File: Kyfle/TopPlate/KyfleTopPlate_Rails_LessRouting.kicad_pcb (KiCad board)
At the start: 2 copper layers, 164 x 146.3 mm, 66 parts, among them SW2 KEY_SWITCH, SW2 PRO MICRO

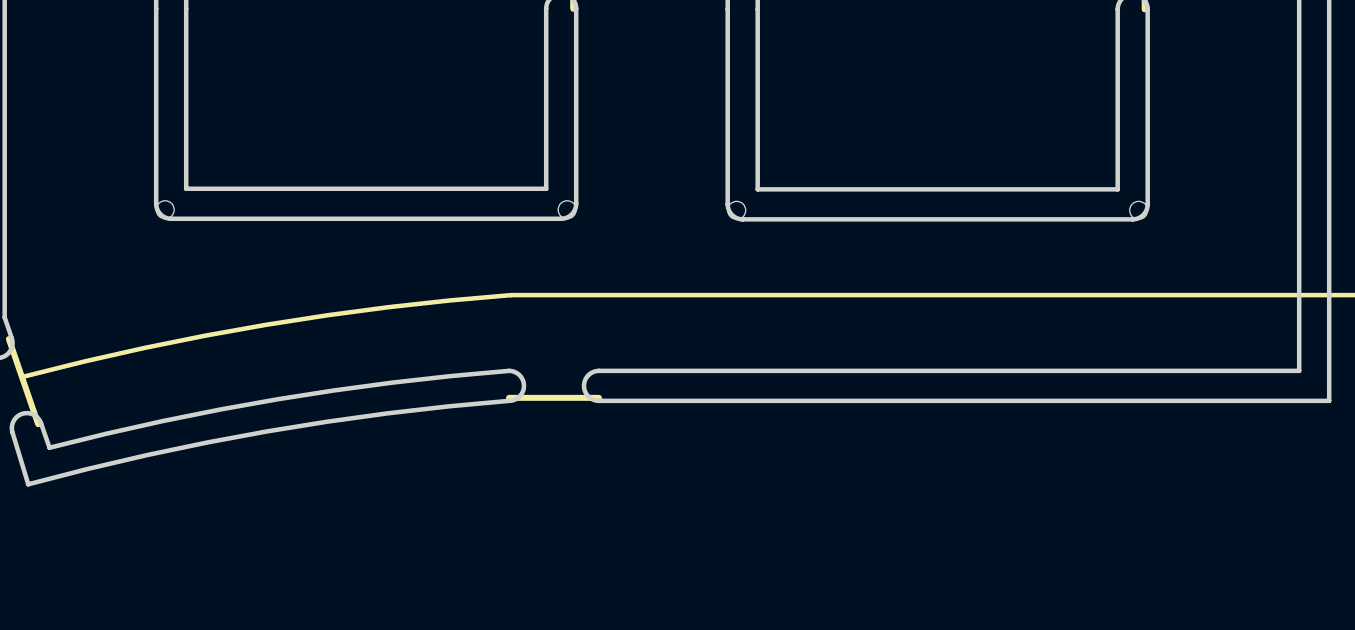
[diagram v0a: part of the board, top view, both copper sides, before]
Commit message: Found a solution to hold slightly better the middle "tongue" of board in the top plate with rails
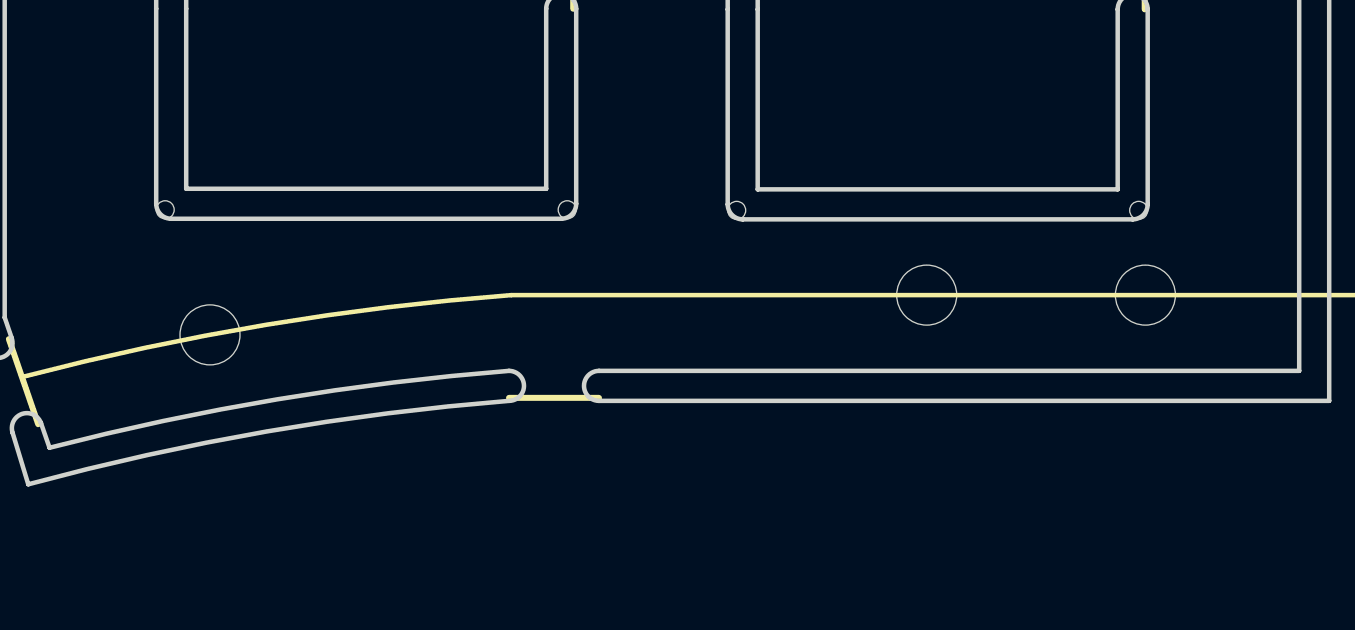
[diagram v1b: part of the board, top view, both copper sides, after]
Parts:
- added REF**: MountingHole_2.2mm_M2_ISO14580, Kyfle Footprints:M2_with_washer, F.Cu at (176.0, 108.6)
- added REF**: MountingHole_2.2mm_M2_ISO14580, Kyfle Footprints:M2_with_washer, F.Cu at (168.7, 108.6)
- added REF**: MountingHole_2.2mm_M2_ISO14580, Kyfle Footprints:M2_with_washer, F.Cu at (144.8, 109.9)
- added SW2: KEY_SWITCH, Kyfle Footprints:CherryMX_Kyfle_v1_TopPlate_1u_Rail_Helper, F.Cu at (140.6, 120.9)
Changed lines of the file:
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@@
     (tracks 0)
     (zones 0)
-    (modules 66)
+    (modules 70)
     (nets 1)
   )
@@
     (44 Edge.Cuts user)
     (45 Margin user hide)
-    (46 B.CrtYd user hide)
-    (47 F.CrtYd user)
+    (46 B.CrtYd user)
+    (47 F.CrtYd user hide)
     (48 B.Fab user hide)
     (49 F.Fab user hide)
@@
     (pad_to_mask_clearance 0)
     (aux_axis_origin 0 0)
-    (grid_origin 161.760381 199.9936)
+    (grid_origin 144.793444 109.920811)
     (visible_elements 7FFFFF7F)
     (pcbplotparams
@@
   )
   (module "Kyfle Footprints:M2_with_washer" (layer F.Cu)
+    (at 175.97375 108.595)
+    (descr "Mounting Hole 2.2mm, no annular, M2, ISO14580")
+    (tags "mounting hole 2.2mm no annular m2 iso14580")
+    (attr virtual)
+    (fp_text reference REF** (at 0 -2.9) (layer B.Fab) hide
+      (effects (font (size 1 1) (thickness 0.15)))
+    )
+    (fp_text value MountingHole_2.2mm_M2_ISO14580 (at 0 2.9) (layer F.Fab)
+      (effects (font (size 1 1) (thickness 0.15)))
+    )
+    (fp_text user %R (at 0.3 0) (layer F.Fab)
+      (effects (font (size 1 1) (thickness 0.15)))
+    )
+    (fp_circle (center 0 0) (end 2 0) (layer F.CrtYd) (width 0.05))
+    (fp_circle (center 0 0) (end 1.6 0) (layer B.CrtYd) (width 0.05))
+    (pad "" np_thru_hole circle (at 0 0) (size 2 2) (drill 2) (layers *.Cu *.Mask)
+      (clearance 1.1))
+  )
+  (module "Kyfle Footprints:M2_with_washer" (layer F.Cu)
+    (at 168.68375 108.595)
+    (descr "Mounting Hole 2.2mm, no annular, M2, ISO14580")
+    (tags "mounting hole 2.2mm no annular m2 iso14580")
+    (attr virtual)
+    (fp_text reference REF** (at 0 -2.9) (layer B.Fab) hide
+      (effects (font (size 1 1) (thickness 0.15)))
+    )
+    (fp_text value MountingHole_2.2mm_M2_ISO14580 (at 0 2.9) (layer F.Fab)
+      (effects (font (size 1 1) (thickness 0.15)))
+    )
+    (fp_text user %R (at 0.3 0) (layer F.Fab)
+      (effects (font (size 1 1) (thickness 0.15)))
+    )
+    (fp_circle (center 0 0) (end 2 0) (layer F.CrtYd) (width 0.05))
+    (fp_circle (center 0 0) (end 1.6 0) (layer B.CrtYd) (width 0.05))
+    (pad "" np_thru_hole circle (at 0 0) (size 2 2) (drill 2) (layers *.Cu *.Mask)
+      (clearance 1.1))
+  )
+  (module "Kyfle Footprints:M2_with_washer" (layer F.Cu)
+    (at 144.793444 109.920811)
+    (descr "Mounting Hole 2.2mm, no annular, M2, ISO14580")
+    (tags "mounting hole 2.2mm no annular m2 iso14580")
+    (attr virtual)
+    (fp_text reference REF** (at 0 -2.9) (layer B.Fab) hide
+      (effects (font (size 1 1) (thickness 0.15)))
+    )
+    (fp_text value MountingHole_2.2mm_M2_ISO14580 (at 0 2.9) (layer F.Fab)
+      (effects (font (size 1 1) (thickness 0.15)))
+    )
+    (fp_text user %R (at 0.3 0) (layer F.Fab)
+      (effects (font (size 1 1) (thickness 0.15)))
+    )
+    (fp_circle (center 0 0) (end 2 0) (layer F.CrtYd) (width 0.05))
+    (fp_circle (center 0 0) (end 1.6 0) (layer B.CrtYd) (width 0.05))
+    (pad "" np_thru_hole circle (at 0 0) (size 2 2) (drill 2) (layers *.Cu *.Mask)
+      (clearance 1.1))
+  )
+  (module "Kyfle Footprints:M2_with_washer" (layer F.Cu)
     (at 105.5 99)
     (descr "Mounting Hole 2.2mm, no annular, M2, ISO14580")
@@
     )
     (fp_circle (center 0 0) (end 2 0) (layer F.CrtYd) (width 0.05))
+    (fp_circle (center 0 0) (end 1.6 0) (layer B.CrtYd) (width 0.05))
     (pad "" np_thru_hole circle (at 0 0) (size 2 2) (drill 2) (layers *.Cu *.Mask)
       (clearance 1.1))
@@
       (effects (font (size 1 1) (thickness 0.15)))
     )
-    (fp_circle (center 0 0) (end 2 0) (layer F.CrtYd) (width 0.05))
-    (fp_text user %R (at 0.3 0) (layer F.Fab)
-      (effects (font (size 1 1) (thickness 0.15)))
-    )
-    (pad "" np_thru_hole circle (at 0 0) (size 2 2) (drill 2) (layers *.Cu *.Mask)
-      (clearance 1.1))
+    (fp_text user %R (at 0.3 0) (layer F.Fab)
+      (effects (font (size 1 1) (thickness 0.15)))
+    )
+    (fp_circle (center 0 0) (end 2 0) (layer F.CrtYd) (width 0.05))
+    (fp_circle (center 0 0) (end 1.6 0) (layer B.CrtYd) (width 0.05))
+    (pad "" np_thru_hole circle (at 0 0) (size 2 2) (drill 2) (layers *.Cu *.Mask)
+      (clearance 1.1))
+  )
+  (module "Kyfle Footprints:CherryMX_Kyfle_v1_TopPlate_1u_Rail_Helper" (layer F.Cu)
+    (at 140.570866 120.913253 15)
+    (fp_text reference SW2 (at 0 3 15) (layer F.Fab) hide
+      (effects (font (size 1 1) (thickness 0.15)))
+    )
+    (fp_text value KEY_SWITCH (at 0 -3 15) (layer F.Fab) hide
+      (effects (font (size 1 1) (thickness 0.15)))
+    )
+    (fp_line (start 0 7) (end 0 7.4) (layer Eco2.User) (width 0.05))
+    (fp_circle (center 6.92375 -9.525) (end 7.92375 -9.525) (layer B.CrtYd) (width 0.12))
+    (fp_circle (center -6.92375 9.525) (end -5.92375 9.525) (layer B.CrtYd) (width 0.12))
+    (fp_circle (center 6.92375 9.525) (end 7.92375 9.525) (layer B.CrtYd) (width 0.12))
+    (fp_line (start -7 7) (end -7 -7) (layer Eco2.User) (width 0.05))
+    (fp_line (start 7 7) (end -7 7) (layer Eco2.User) (width 0.05))
+    (fp_line (start 7 -7) (end 7 7) (layer Eco2.User) (width 0.05))
+    (fp_line (start -7 -7) (end 7 -7) (layer Eco2.User) (width 0.05))
+    (fp_line (start -9.025 9.025) (end -9.025 -9.025) (layer B.CrtYd) (width 0.12))
+    (fp_line (start 9.025 9.025) (end -9.025 9.025) (layer B.CrtYd) (width 0.12))
+    (fp_line (start 9.025 -9.025) (end 9.025 9.025) (layer B.CrtYd) (width 0.12))
+    (fp_line (start -9.025 -9.025) (end 9.025 -9.025) (layer B.CrtYd) (width 0.12))
+    (fp_line (start 9.525 -9.525) (end -9.525 -9.525) (layer F.Fab) (width 0.15))
+    (fp_line (start -9.525 -9.525) (end -9.525 9.525) (layer F.Fab) (width 0.15))
+    (fp_line (start -9.525 9.525) (end 9.525 9.525) (layer F.Fab) (width 0.15))
+    (fp_line (start 9.525 9.525) (end 9.525 -9.525) (layer F.Fab) (width 0.15))
+    (fp_line (start -7.8 -7.8) (end 7.8 -7.8) (layer F.CrtYd) (width 0.12))
+    (fp_line (start 7.8 -7.8) (end 7.8 7.8) (layer F.CrtYd) (width 0.12))
+    (fp_line (start 7.8 7.8) (end -7.8 7.8) (layer F.CrtYd) (width 0.12))
+    (fp_line (start -7.8 7.8) (end -7.8 -7.8) (layer F.CrtYd) (width 0.12))
+    (fp_circle (center -6.92375 -9.525) (end -5.92375 -9.525) (layer B.CrtYd) (width 0.12))
+    (fp_circle (center 6.7 -6.7) (end 7 -6.7) (layer Eco2.User) (width 0.05))
+    (fp_circle (center -6.7 -6.7) (end -6.4 -6.7) (layer Eco2.User) (width 0.05))
+    (fp_circle (center 6.7 6.7) (end 7 6.7) (layer Eco2.User) (width 0.05))
+    (fp_circle (center -6.7 6.7) (end -6.4 6.7) (layer Eco2.User) (width 0.05))
+    (model ${ACHERONLIB}/3d_models/mx_switch.step
+      (offset (xyz -7.35 -7.3 0))
+      (scale (xyz 1 1 1))
+      (rotate (xyz -90 0 0))
+    )
   )
   (module "Kyfle Footprints:SK6812_Bit_Bottom" (layer F.Cu)

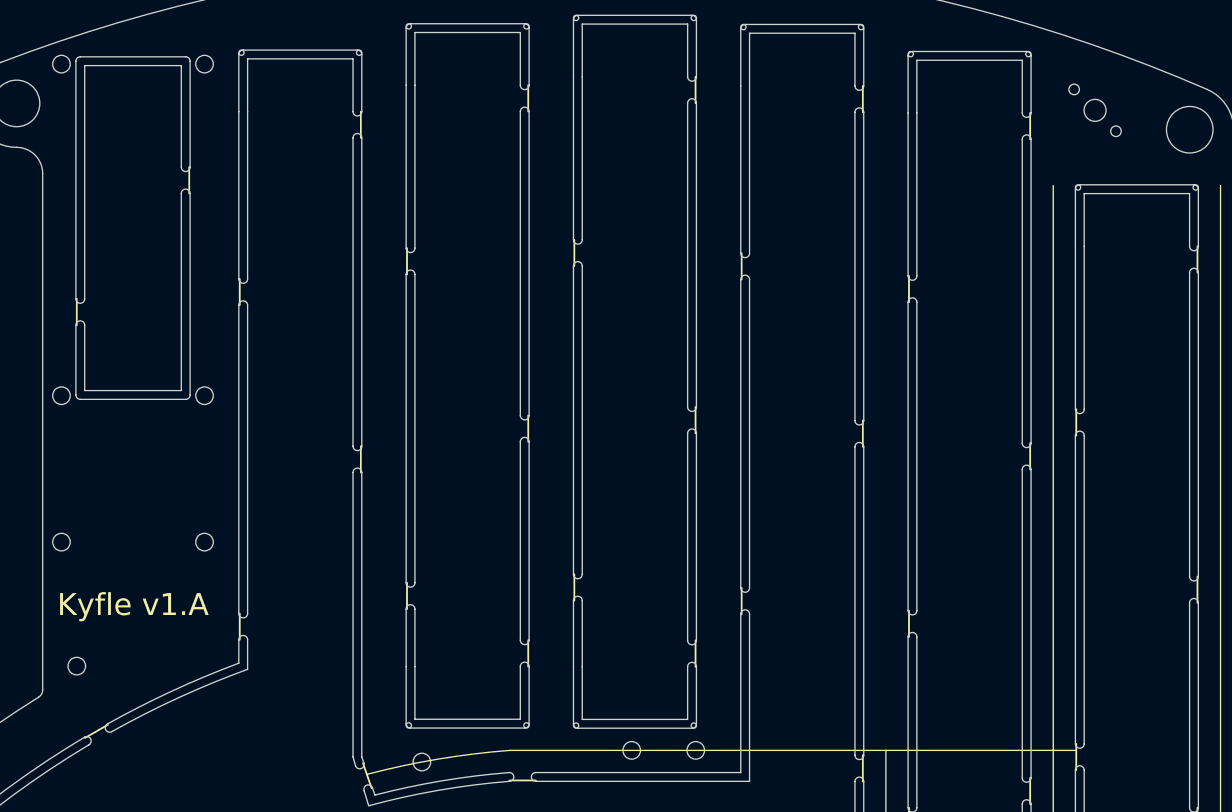
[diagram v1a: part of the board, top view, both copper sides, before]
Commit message: Plates: Received M2 and M5 hardware. It's bigger than specified...
- M5 screw head is ~9.5 instead of 8.7. Was colliding in the top left 
corner with M2 screw for pro micro board. So I shifted up pro micro 
board 0.3mm.
- M2 screw head is also larger than expected (3.8 instead of 3.2). But 
it is mostly fine as I was designing with 4-4.2mm clearance. Only 
exception was for screws supporting the middle bottom section of top 
plate with rails. Here it was colliding with switch housing. So, only 
solution is to use so called reduced slotted screws (DIN 920) as they 
have 2.8mm diameter head.
- Also added JLCPCB silk reference
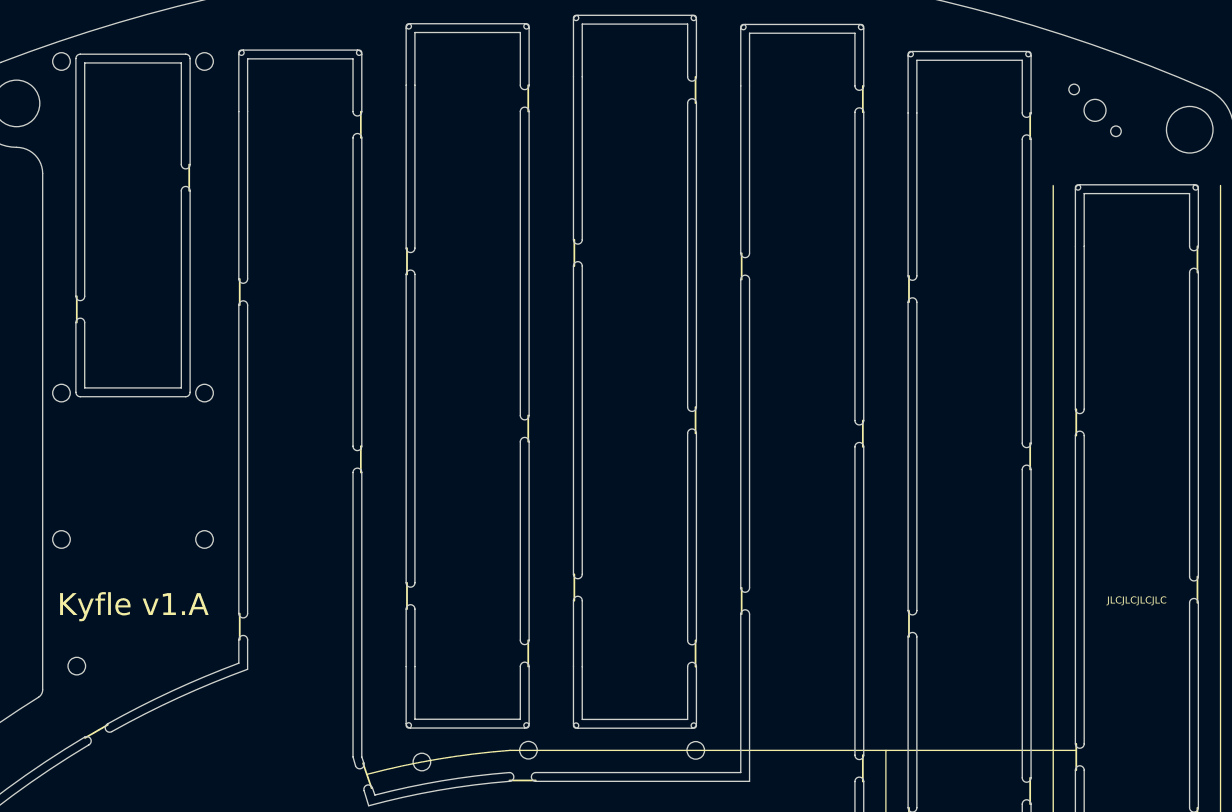
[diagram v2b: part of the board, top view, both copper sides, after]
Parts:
- added JLCJLCJLCJLC: JLCBCB_OrderNumber, Kyfle Footprints:JLCBCB_OrderNumber, F.Cu at (226.2, 91.5)
- moved REF** 11.8 mm to (156.9, 108.6)
- moved SW2 0.30 mm to (111.9, 58.4)
